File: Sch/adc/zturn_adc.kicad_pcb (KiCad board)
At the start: 4 copper layers, 89.5 x 80 mm, 111 parts, among them CN1 SMA, CN2 SMA, CN3 AudioJack, J1 JP4, J2 Header5, J3 JP2, J4 JP2, J5 JP2, J6 JP2, J7 JP2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

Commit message: done except GND net
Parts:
- removed J7: JP2, adc_lib:M20-9980245
- added C48: 1uF, adc_lib:C0603, F.Cu at (158.2, 74.6)
- added C49: 1uF, adc_lib:C0603, F.Cu at (157.0, 69.0)
- added L10: L, adc_lib:FB0805, F.Cu at (155.5, 72.0)
- added L11: L, adc_lib:FB0805, F.Cu at (150.1, 116.5)
- added L7: L, adc_lib:FB0805, F.Cu at (162.2, 74.6)
- added R3: 10k, adc_lib:R0603, F.Cu at (163.7, 71.1)
- added U7: TLV702, adc_lib:TLV702, F.Cu at (160.2, 71.1)
- moved L8 7.31 mm to (141.5, 75.0), turned to 135 degrees
- moved C45 0.07 mm to (148.5, 69.0)
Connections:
- net Net-(C46-Pad1) renamed /AudioDAC/VDDC
- C12 pad 1: /RF_in/VCC -> Net-(C12-Pad1)
- C25 pad 2: /RF_in/VCC -> Net-(C25-Pad2)
- L5 pad 1: /RF_in/VCC -> Net-(C25-Pad2)
- U2 pad 1: /RF_in/VCC -> Net-(C25-Pad2)
- U4 pad 1: /RF_in/VCC -> Net-(C12-Pad1)
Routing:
- net GND: track 24.6 -> 68.2 mm, vias 2 -> 7
- net Net-(C28-Pad1): track 15.5 -> 41.3 mm, vias 1 -> 3
- net Net-(C18-Pad1): track 21.7 -> 33.6 mm, vias 4 -> 3
- net /AudioDAC/VDDC: track 16.3 -> 7.88 mm, vias 2 -> 3
- net Net-(C48-Pad1): track 0.00 -> 6.99 mm
- net /RF_in/VCC: track 6.85 -> 0.00 mm, vias 1 -> 0
- net VDD3: track 18.6 -> 24.4 mm, vias 3 -> 4
- net Net-(C12-Pad1): track 0.00 -> 5.70 mm, vias 0 -> 2
- net Net-(C49-Pad1): track 0.00 -> 4.71 mm
- net +3V3: track 25.7 -> 30.3 mm, vias 9 -> 11
- net Net-(C25-Pad2): track 0.00 -> 4.28 mm
- net Net-(R3-Pad2): track 0.00 -> 2.24 mm
- net /RF_in/VCC33: track 14.8 -> 16.6 mm, vias 2 -> 3
- net /CN/SHDNB: track 45.2 -> 46.6 mm
- added copper zone on In2.Cu, net /AudioDAC/VDDC
- added copper zone on In2.Cu, net /RF_in/VCC33

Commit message: Apply some design rules
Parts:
- moved L9 2.29 mm to (115.9, 116.1), turned to 135 degrees
- moved C33 1.39 mm to (134.7, 100.4)
- moved C34 1.34 mm to (135.4, 101.2)
- moved C36 1.23 mm to (140.1, 105.0)
- moved C35 1.22 mm to (139.3, 104.3)
- moved C32 0.88 mm to (140.8, 103.7)
- moved C31 0.75 mm to (136.2, 99.7)
- moved C30 0.44 mm to (141.5, 102.9)
- moved C29 0.41 mm to (137.1, 98.7)
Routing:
- net Net-(C18-Pad1): track 33.6 -> 31.3 mm, vias 3 -> 2
- net Net-(C29-Pad1): track 6.55 -> 5.10 mm
- net Net-(C30-Pad2): track 5.94 -> 4.55 mm
- net Net-(C30-Pad1): track 5.96 -> 4.61 mm
- net Net-(C29-Pad2): track 6.59 -> 5.24 mm
- net /CN/MUX: track 59.1 -> 60.1 mm
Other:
- net class Power added: clearance 0.2, trace_width 0.6, via_dia 0.6, via_drill 0.4
- net class Power2 added: clearance 0.2, trace_width 0.4, via_dia 0.6, via_drill 0.4

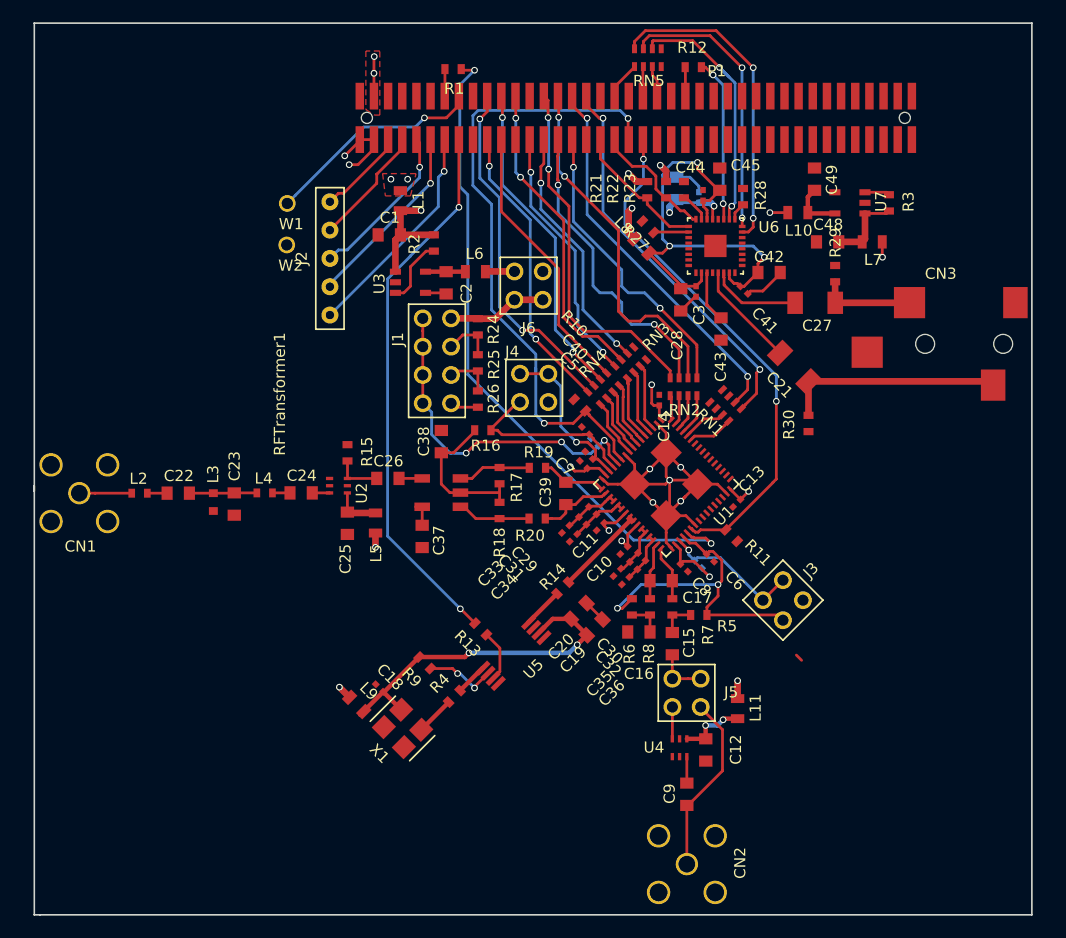
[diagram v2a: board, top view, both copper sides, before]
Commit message: Changed footprint for the Audio DAC. Silk arrangement
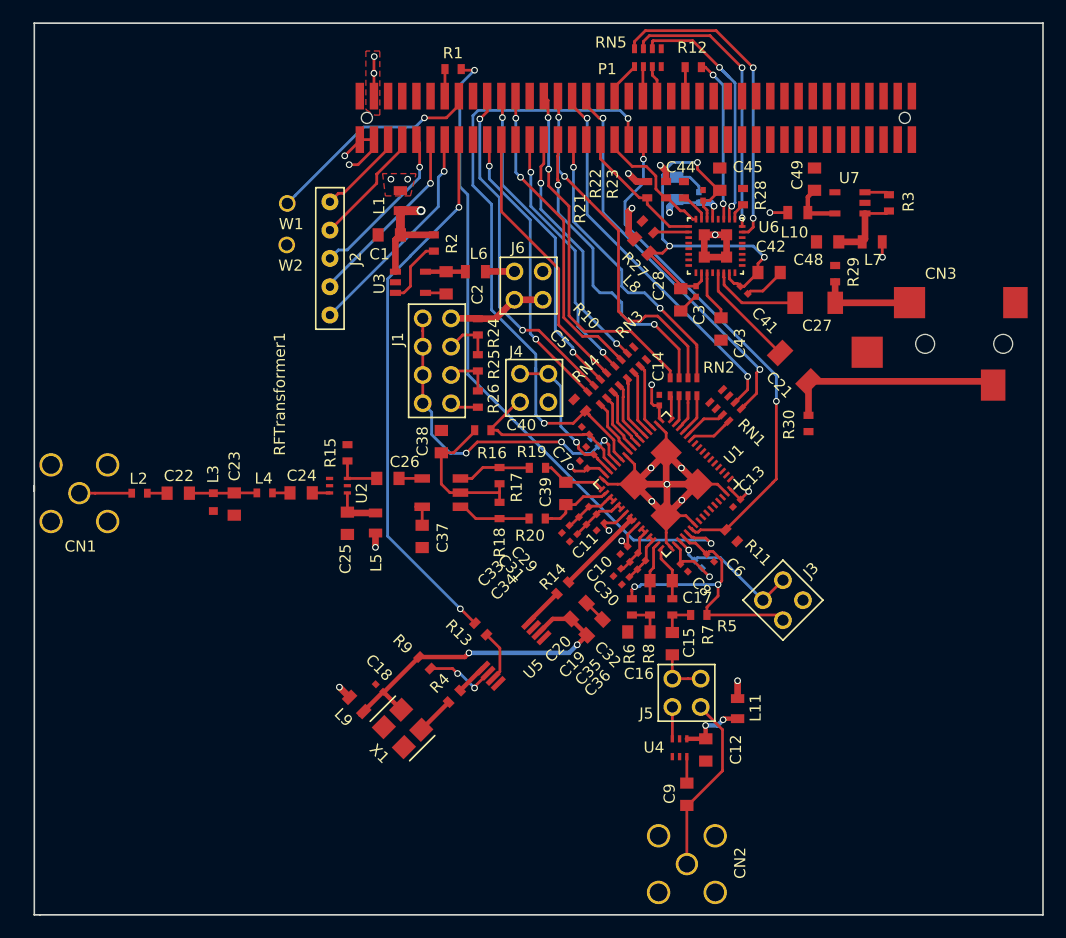
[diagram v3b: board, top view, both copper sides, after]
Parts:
- moved C5 0.42 mm to (136.8, 93.4)
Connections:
- U6 pad 33: (no net) -> GND
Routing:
- net GND: track 68.6 -> 76.1 mm, vias 7 -> 8
- net /RF_in/VCMB: track 27.9 -> 25.1 mm
- net (no net): track 0.67 -> 0.00 mm
- net Net-(C5-Pad1): track 14.6 -> 14.1 mm
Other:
- board size 89.5 x 80 mm -> 90.5 x 80 mm
- net class Power3 added: clearance 0.2, trace_width 0.8, via_dia 0.8, via_drill 0.5

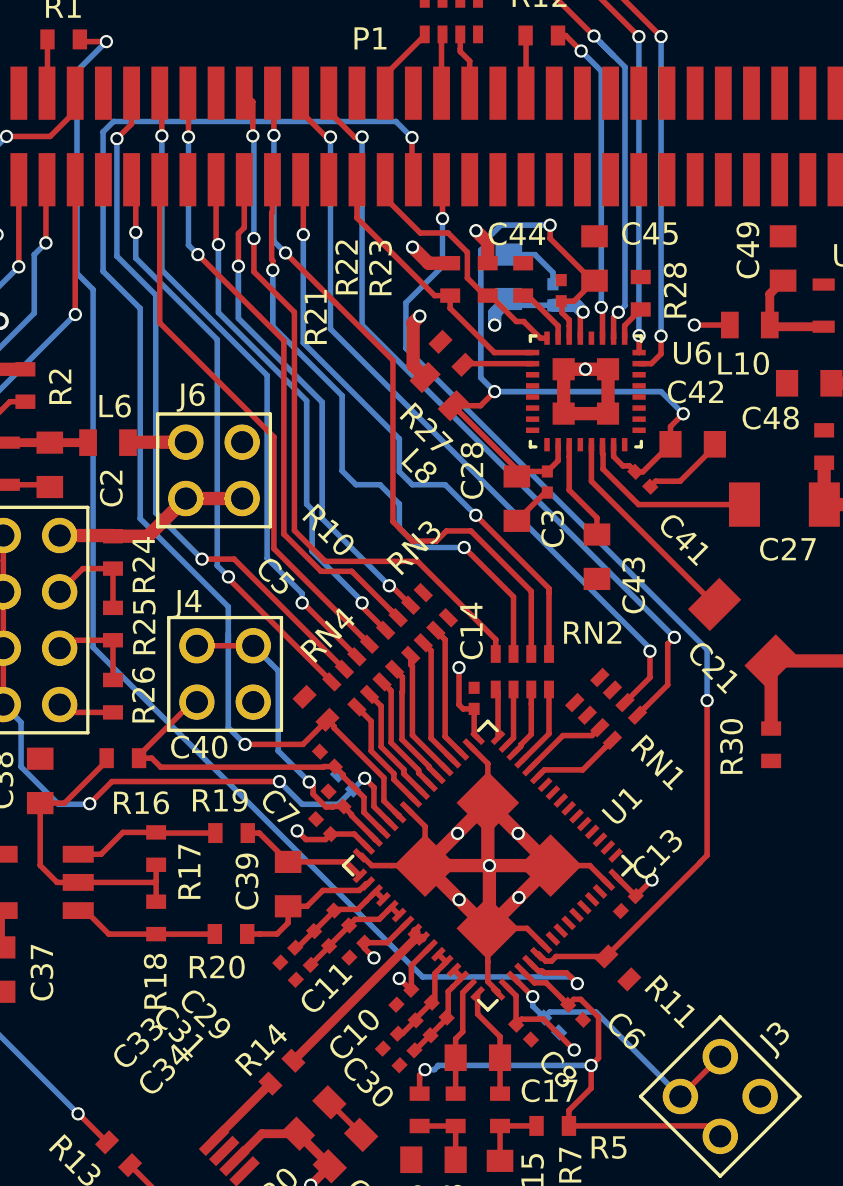
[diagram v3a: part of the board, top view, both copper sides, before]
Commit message: length matched within 3.63mm on ADC output
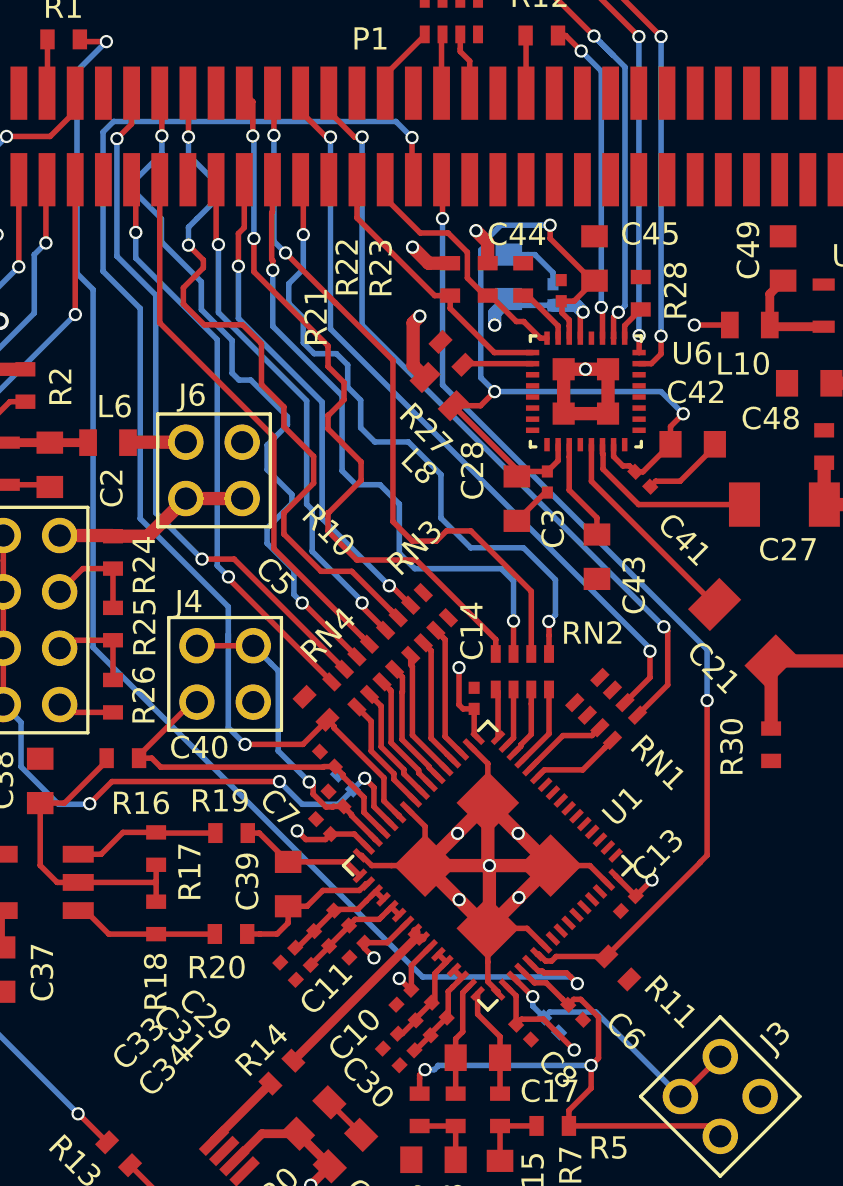
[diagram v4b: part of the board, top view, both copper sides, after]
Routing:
- net /CN/IO_B13_LN15: track 28.9 -> 32.7 mm
- net /CN/IO_B13_LP15: track 29.1 -> 32.1 mm
- net /CN/IO_B34_LN3: track 26.9 -> 29.7 mm
- net /CN/SHDNB: track 46.6 -> 45.2 mm
- net /CN/IO_B34_LP3: track 27.7 -> 28.8 mm
- net /CN/IO_B34_LP2: track 32.4 -> 33.4 mm
